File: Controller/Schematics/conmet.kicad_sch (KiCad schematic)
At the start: 12 parts, among them Q1 FQU20N06L, U1 RGBW_Led_Strip, U2 MP1584EN, U3 JS202011AQN, U4 VL53L1X

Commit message: added button code to controller (no sensor only)
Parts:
- added R?: 10K, symbol Device:R_US
- added SW?: SW_Push, symbol Switch:SW_Push
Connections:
- net +5V: now also SW?.2
- net Earth: now also R?.1
- net at A1.8 (D5): now also R?.2, SW?.1
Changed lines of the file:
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@@
 (kicad_sch (version 20211123) (generator eeschema)
   (paper "A4")
+  (junction (at 215.265 102.87) (diameter 0) (color 0 0 0 0)
+  )
   (junction (at 213.995 73.025) (diameter 0) (color 0 0 0 0)
   )
@@
     (stroke (width 0) (type default) (color 0 0 0 0))
   )
+  (wire (pts (xy 205.74 78.105) (xy 205.74 102.87))
+    (stroke (width 0) (type default) (color 0 0 0 0))
+  )
   (wire (pts (xy 56.515 88.9) (xy 56.515 95.885))
     (stroke (width 0) (type default) (color 0 0 0 0))
@@
     (stroke (width 0) (type default) (color 0 0 0 0))
   )
+  (wire (pts (xy 240.03 97.79) (xy 240.03 102.87))
+    (stroke (width 0) (type default) (color 0 0 0 0))
+  )
   (wire (pts (xy 114.3 123.825) (xy 114.3 126.365))
     (stroke (width 0) (type default) (color 0 0 0 0))
   )
+  (wire (pts (xy 240.03 102.87) (xy 228.6 102.87))
+    (stroke (width 0) (type default) (color 0 0 0 0))
+  )
   (wire (pts (xy 226.695 78.105) (xy 226.695 88.9))
     (stroke (width 0) (type default) (color 0 0 0 0))
@@
     (stroke (width 0) (type default) (color 0 0 0 0))
   )
+  (wire (pts (xy 205.74 102.87) (xy 215.265 102.87))
+    (stroke (width 0) (type default) (color 0 0 0 0))
+  )
   (wire (pts (xy 134.62 113.665) (xy 127 113.665))
     (stroke (width 0) (type default) (color 0 0 0 0))
@@
     (stroke (width 0) (type default) (color 0 0 0 0))
   )
+  (wire (pts (xy 215.265 113.665) (xy 215.265 118.11))
+    (stroke (width 0) (type default) (color 0 0 0 0))
+  )
   (wire (pts (xy 127 71.12) (xy 127 74.93))
     (stroke (width 0) (type default) (color 0 0 0 0))
@@
     (stroke (width 0) (type default) (color 0 0 0 0))
   )
+  (wire (pts (xy 194.945 78.105) (xy 205.74 78.105))
+    (stroke (width 0) (type default) (color 0 0 0 0))
+  )
   (wire (pts (xy 114.3 105.41) (xy 114.3 106.045))
     (stroke (width 0) (type default) (color 0 0 0 0))
@@
     (stroke (width 0) (type default) (color 0 0 0 0))
   )
+  (wire (pts (xy 215.265 102.87) (xy 218.44 102.87))
+    (stroke (width 0) (type default) (color 0 0 0 0))
+  )
   (wire (pts (xy 148.59 107.315) (xy 148.59 109.22))
     (stroke (width 0) (type default) (color 0 0 0 0))
@@
   )
   (wire (pts (xy 219.075 73.025) (xy 213.995 73.025))
+    (stroke (width 0) (type default) (color 0 0 0 0))
+  )
+  (wire (pts (xy 215.265 106.045) (xy 215.265 102.87))
     (stroke (width 0) (type default) (color 0 0 0 0))
   )
@@
     )
     (pin "1")
+  )
+  (symbol (lib_id "Switch:SW_Push") (at 223.52 102.87 0) (unit 1)
+    (in_bom yes) (on_board yes) (fields_autoplaced)
+    (property "Reference" "SW?" (id 0) (at 223.52 95.25 0))
+    (property "Value" "SW_Push" (id 1) (at 223.52 97.79 0))
+    (property "Footprint" "" (id 2) (at 223.52 97.79 0)
+      (effects (font (size 1.27 1.27)) hide)
+    )
+    (property "Datasheet" "~" (id 3) (at 223.52 97.79 0)
+      (effects (font (size 1.27 1.27)) hide)
+    )
+    (pin "1")
+    (pin "2")
   )
   (symbol (lib_id "MCU_Module:Arduino_Nano_Every") (at 182.245 83.185 0) (mirror y) (unit 1)
@@
     (pin "1")
   )
+  (symbol (lib_id "power:Earth") (at 215.265 118.11 0) (mirror y) (unit 1)
+    (in_bom yes) (on_board yes) (fields_autoplaced)
+    (property "Reference" "#PWR?" (id 0) (at 215.265 124.46 0)
+      (effects (font (size 1.27 1.27)) hide)
+    )
+    (property "Value" "Earth" (id 1) (at 215.265 121.92 0)
+      (effects (font (size 1.27 1.27)) hide)
+    )
+    (property "Footprint" "" (id 2) (at 215.265 118.11 0)
+      (effects (font (size 1.27 1.27)) hide)
+    )
+    (property "Datasheet" "~" (id 3) (at 215.265 118.11 0)
+      (effects (font (size 1.27 1.27)) hide)
+    )
+    (pin "1")
+  )
   (symbol (lib_id "power:Earth") (at 61.595 95.885 0) (unit 1)
     (in_bom yes) (on_board yes) (fields_autoplaced)
@@
     (pin "")
   )
+  (symbol (lib_id "power:+5V") (at 240.03 97.79 0) (unit 1)
+    (in_bom yes) (on_board yes) (fields_autoplaced)
+    (property "Reference" "#PWR?" (id 0) (at 240.03 101.6 0)
+      (effects (font (size 1.27 1.27)) hide)
+    )
+    (property "Value" "+5V" (id 1) (at 240.03 92.71 0))
+    (property "Footprint" "" (id 2) (at 240.03 97.79 0)
+      (effects (font (size 1.27 1.27)) hide)
+    )
+    (property "Datasheet" "" (id 3) (at 240.03 97.79 0)
+      (effects (font (size 1.27 1.27)) hide)
+    )
+    (pin "1")
+  )
   (symbol (lib_id "power:+24V") (at 234.315 41.275 0) (mirror y) (unit 1)
     (in_bom yes) (on_board yes) (fields_autoplaced)
@@
     )
     (pin "1")
+  )
+  (symbol (lib_id "Device:R_US") (at 215.265 109.855 0) (mirror x) (unit 1)
+    (in_bom yes) (on_board yes) (fields_autoplaced)
+    (property "Reference" "R?" (id 0) (at 213.36 108.5849 0)
+      (effects (font (size 1.27 1.27)) (justify right))
+    )
+    (property "Value" "10K" (id 1) (at 213.36 111.1249 0)
+      (effects (font (size 1.27 1.27)) (justify right))
+    )
+    (property "Footprint" "" (id 2) (at 216.281 109.601 90)
+      (effects (font (size 1.27 1.27)) hide)
+    )
+    (property "Datasheet" "~" (id 3) (at 215.265 109.855 0)
+      (effects (font (size 1.27 1.27)) hide)
+    )
+    (pin "1")
+    (pin "2")
   )
   (symbol (lib_id "Device:R_US") (at 202.565 136.525 0) (mirror y) (unit 1)
@@
       (reference "#PWR018") (unit 1) (value "Earth") (footprint "")
     )
+    (path "/5955e379-e988-4782-9f51-0a72b4f29d29"
+      (reference "#PWR?") (unit 1) (value "Earth") (footprint "")
+    )
+    (path "/b7915c53-756a-44eb-8426-cebd7a914edc"
+      (reference "#PWR?") (unit 1) (value "+5V") (footprint "")
+    )
     (path "/32567c2a-a5fb-4348-bb27-ff092c103196"
       (reference "A1") (unit 1) (value "Arduino_Nano_Every") (footprint "Module:Arduino_Nano")
@@
       (reference "R5") (unit 1) (value "1k") (footprint "")
     )
+    (path "/c95c576a-10b3-4d71-80db-92da2b733bf5"
+      (reference "R?") (unit 1) (value "10K") (footprint "")
+    )
+    (path "/2fc1b071-38cc-42a2-83a3-c31e7b0831ab"
+      (reference "SW?") (unit 1) (value "SW_Push") (footprint "")
+    )
     (path "/ee0895ff-bec2-4dc0-a9f3-a14c5a497fd0"

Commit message: updates
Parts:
- added D1: LED, symbol Device:LED
- added Q2: FQU20N06L, symbol Device:Q_NMOS_DGS
- added R6: 250, symbol Device:R_US
- added R7: 10K, symbol Device:R_US
- gave numbers to parts that had none: 2
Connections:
- net +24V: now also D1.2 (A)
- net Earth: now also Q2.3 (S), R7.1
- net at A1.9 (D6): now also R6.2
- new net: Q2.1 (G), R6.1, R7.2
- new net: D1.1 (K), Q2.2 (D)
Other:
- note added: "MOMENTARY MANUAL SWITCH w/ 24V LED"
- moved on the sheet: H1, Q1, R1, R2, R3, R4, R5, R8, SW1, U1, U2, U3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

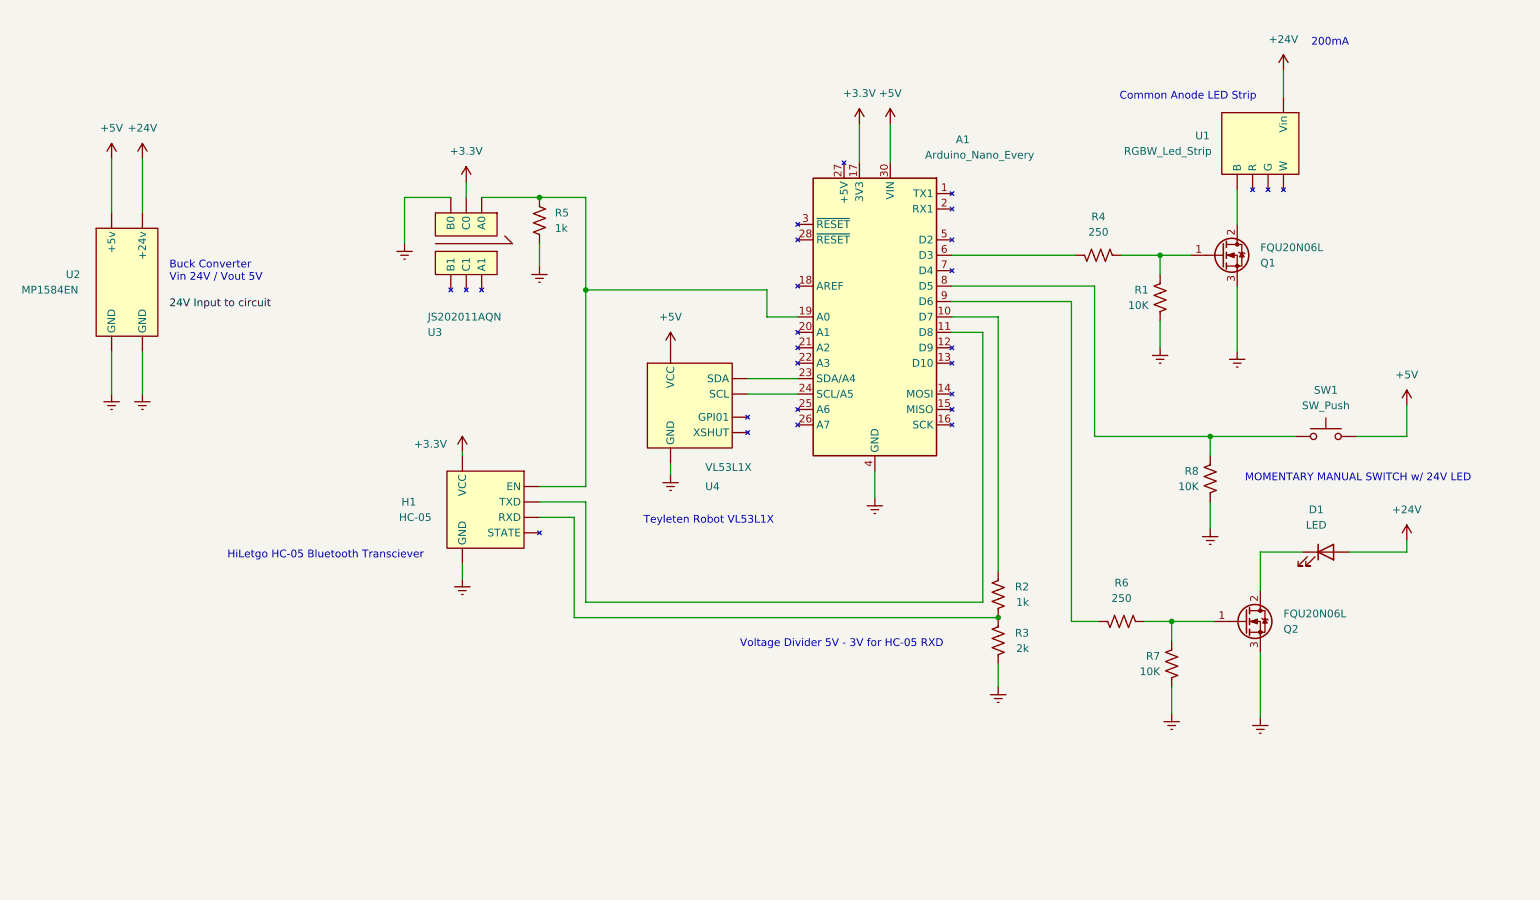
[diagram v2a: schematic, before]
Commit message: updating schmeatics with pcb layout
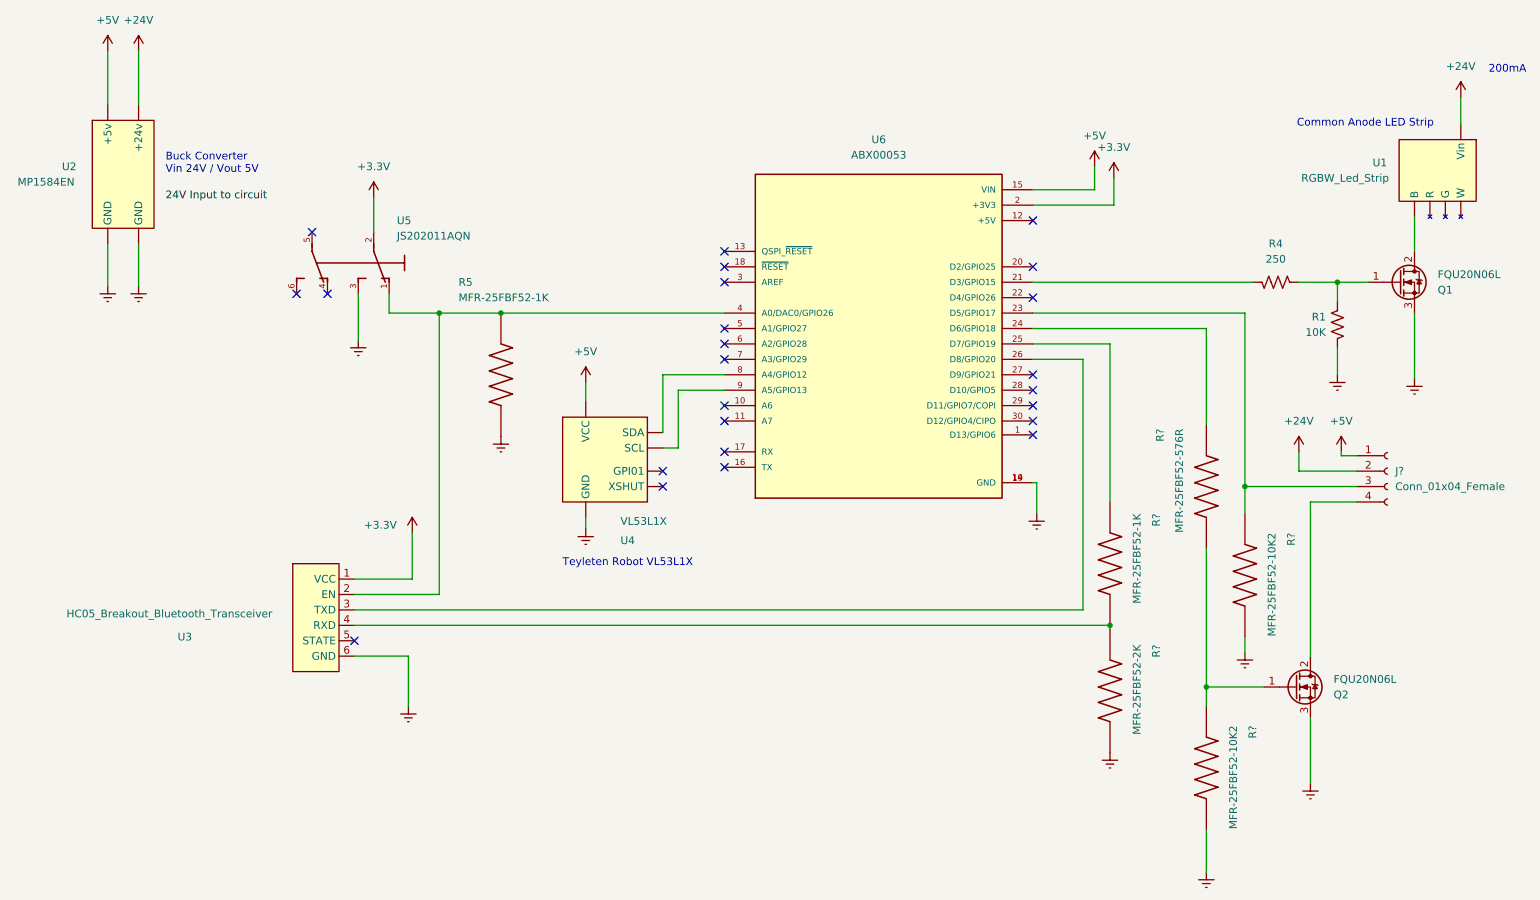
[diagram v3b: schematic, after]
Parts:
- removed A1: Arduino_Nano_Every, Module:Arduino_Nano, symbol MCU_Module:Arduino_Nano_Every
- removed D1: LED, symbol Device:LED
- removed H1: HC-05, symbol New_Library:HC-05
- removed R2, R5: 1k, symbol Device:R_US
- removed R3: 2k, symbol Device:R_US
- removed R6: 250, symbol Device:R_US
- removed R7, R8: 10K, symbol Device:R_US
- removed SW1: SW_Push, symbol Switch:SW_Push
- removed U3: JS202011AQN, symbol New_Library:slide_switch
- added J?: Conn_01x04_Female, Connector_PinSocket_2.54mm:PinSocket_1x04_P2.54mm_Horizontal, symbol Connector:Conn_01x04_Female
- added R5, R?: MFR-25FBF52-1K, MFR-25FBF52-1K_RESAD1100W55L680D260, symbol SnapEDA-Library:MFR-25FBF52-1K
- added R?: MFR-25FBF52-576R, MFR-25FBF52-1K_RESAD1100W55L680D260, symbol SnapEDA-Library:MFR-25FBF52-1K
- added R? (x2): MFR-25FBF52-10K2, MFR-25FBF52-1K_RESAD1100W55L680D260, symbol SnapEDA-Library:MFR-25FBF52-1K
- added R?: MFR-25FBF52-2K, MFR-25FBF52-1K_RESAD1100W55L680D260, symbol SnapEDA-Library:MFR-25FBF52-1K
- added U3: HC05_Breakout_Bluetooth_Transceiver, PrezenzQ:HC05 Breakout Bluetooth Transceiver, symbol PrezenzQ:HC05_Breakout_Bluetooth_Transceiver
- added U5: JS202011AQN, Button_Switch_THT:SW_CuK_JS202011AQN_DPDT_Angled, symbol SnapEDA-Library:JS202011AQN
- added U6: ABX00053, MODULE_ABX00053, symbol SnapEDA-Library:ABX00053
- U2: footprint (none) -> Library:eBoot Mini MP1584EN DC-DC Buck Converter Adjustable Power Supply Module 24V to 12V 9V 5V 3V
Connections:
- net +24V: now also J?.2 (Pin_2)
- net +3V3: now also U3.1 (VCC), U5.2, U6.2 (+3V3)
- net +5V: now also J?.1 (Pin_1), U6.15 (VIN)
- net Earth: now also R5.2, R?.2, R?.2, R?.2, U3.6 (GND), U5.3, U6.14 (GND), U6.19 (GND)
- net at R4.2: now also U6.21 (D3/GPIO15)
- net at Q2.1 (G): now also R?.1, R?.2
- net at Q2.2 (D): now also J?.4 (Pin_4)
- new net: R?.1, U6.25 (D7/GPIO19)
- new net: R?.1, R?.2, U3.4 (RXD)
- new net: J?.3 (Pin_3), R?.1, U6.23 (D5/GPIO17)
- new net: R?.1, U6.24 (D6/GPIO18)
- new net: U3.3 (TXD), U6.26 (D8/GPIO20)
- new net: R5.1, U3.2 (EN), U5.1, U6.4 (A0/DAC0/GPIO26)
- new net: U4. (XSHUT), U6.8 (A4/GPIO12)
- new net: U4. (XSHUT), U6.9 (A5/GPIO13)
- no-connect marks 0 -> 24
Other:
- note removed: "HiLetgo HC-05 Bluetooth Transciever"
- note removed: "MOMENTARY MANUAL SWITCH w/ 24V LED"
- note removed: "Voltage Divider 5V - 3V for HC-05 RXD"
- moved on the sheet: Q1, Q2, R1, R4, U1, U2
